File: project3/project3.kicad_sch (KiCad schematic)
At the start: 1 part

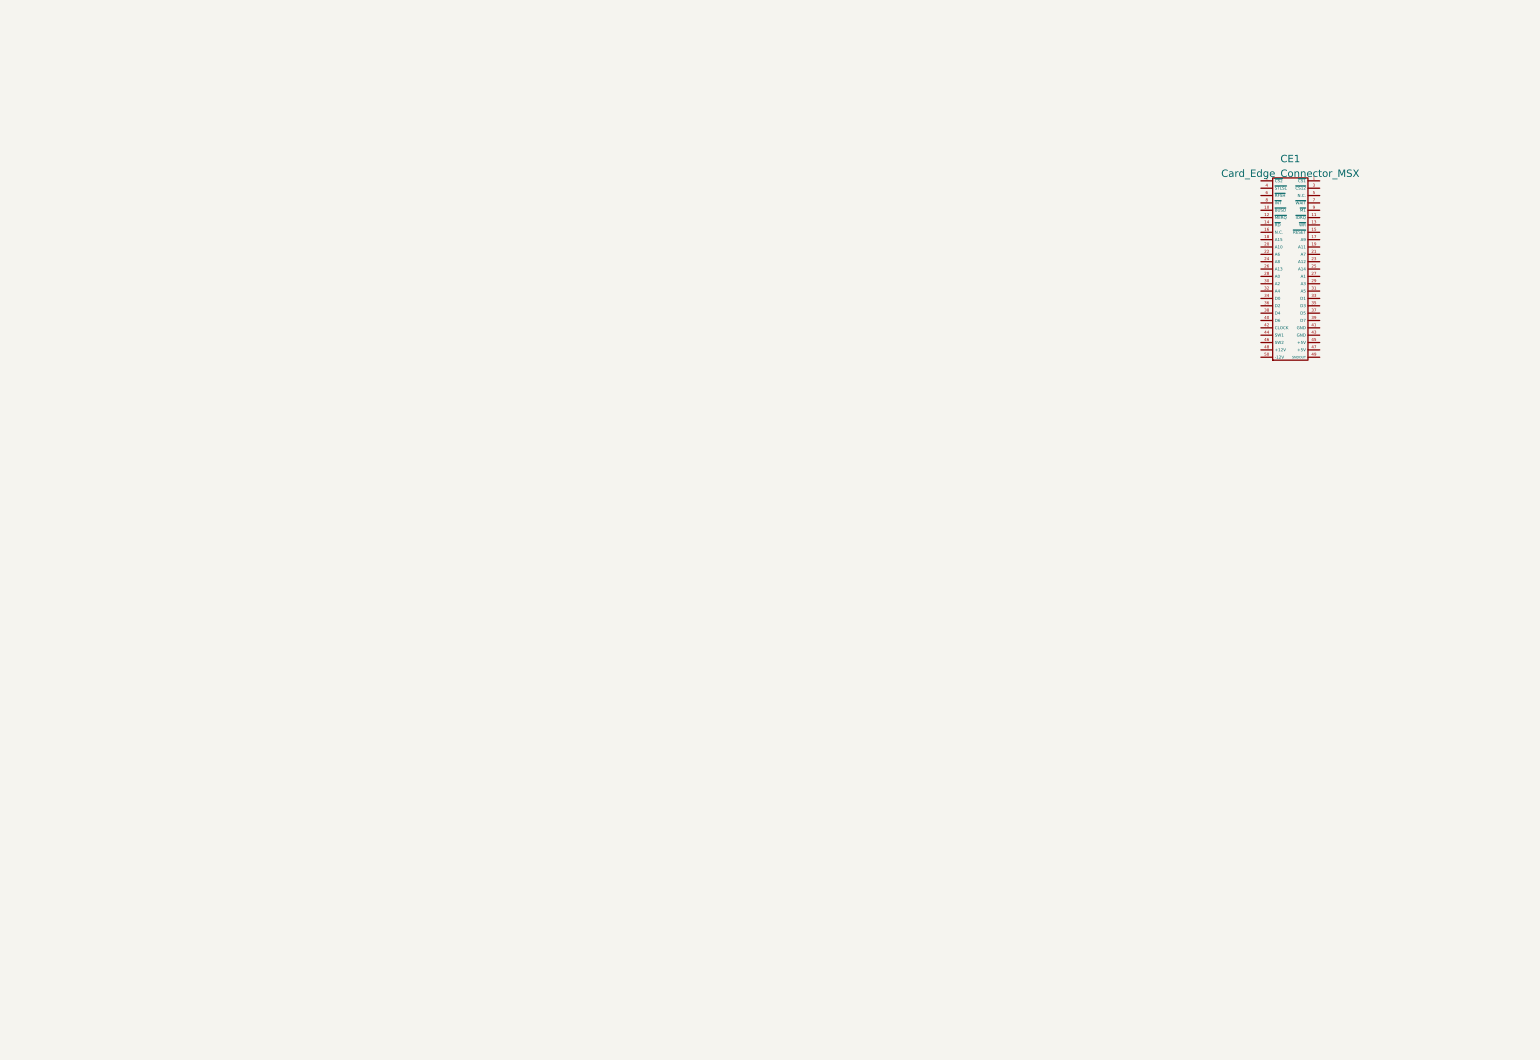
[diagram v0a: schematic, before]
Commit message: Created 4Mega ROM PCB - Change DIP32 type FLASH ROM - Optimal Logic Mega Rom Mapper.
Signed-off-by: Youngki Park <ykp7409@gmail.com>
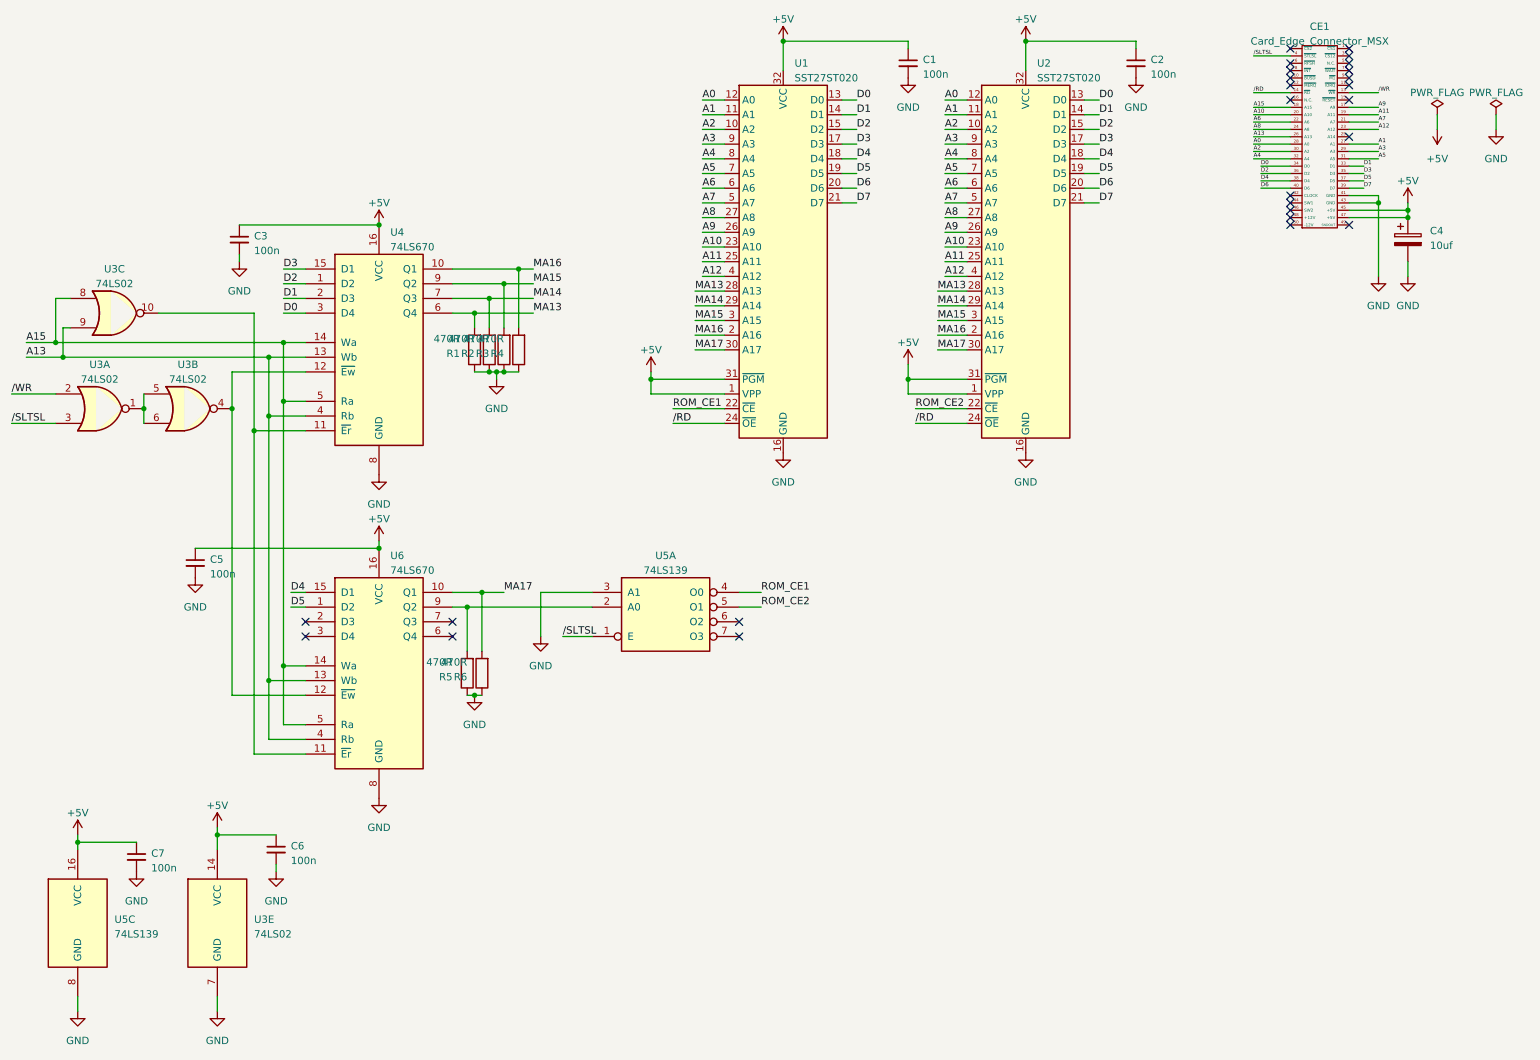
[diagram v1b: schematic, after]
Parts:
- added C1, C2, C3, C5, C6, C7: 100n, Capacitor_THT:C_Disc_D6.0mm_W2.5mm_P5.00mm, symbol Device:C_Small
- added C4: 10uf, Capacitor_THT:CP_Radial_D5.0mm_P2.50mm, symbol Device:C_Polarized
- added R1, R2, R3, R4, R5, R6: 470R, Resistor_THT:R_Axial_DIN0207_L6.3mm_D2.5mm_P10.16mm_Horizontal, symbol Device:R
- added U1, U2: SST27ST020, Package_DIP:DIP-32_W15.24mm_Socket, symbol Memory_Flash_Custom:SST27ST020
- added U3: 74LS02, Package_DIP:DIP-14_W7.62mm_Socket, symbol 74xx:74LS02
- added U4, U6: 74LS670, Package_DIP:DIP-16_W7.62mm_Socket, symbol 74xx:74LS670
- added U5: 74LS139, Package_DIP:DIP-16_W7.62mm_Socket, symbol 74xx:74LS139
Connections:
- net /WR: now reaches CE1.13 (~{WR})
- net /WR: now also U3.2
- net /RD: now reaches CE1.14 (~{RD})
- net /RD: now also U1.24 (~{OE}), U2.24 (~{OE})
- net A9: now reaches CE1.17 (A9)
- net A9: now also U1.26 (A9), U2.26 (A9)
- net A15: now reaches CE1.18 (A15)
- net A15: now also U3.8, U4.14 (Wa), U4.5 (Ra), U6.14 (Wa), U6.5 (Ra)
- net A11: now reaches CE1.19 (A11)
- net A11: now also U1.25 (A11), U2.25 (A11)
- net A10: now reaches CE1.20 (A10)
- net A10: now also U1.23 (A10), U2.23 (A10)
- net A7: now reaches CE1.21 (A7)
- net A7: now also U1.5 (A7), U2.5 (A7)
- net A6: now reaches CE1.22 (A6)
- net A6: now also U1.6 (A6), U2.6 (A6)
- net A12: now reaches CE1.23 (A12)
- net A12: now also U1.4 (A12), U2.4 (A12)
- net A8: now reaches CE1.24 (A8)
- net A8: now also U1.27 (A8), U2.27 (A8)
- net A13: now reaches CE1.26 (A13)
- net A13: now also U3.9, U4.13 (Wb), U4.4 (Rb), U6.13 (Wb), U6.4 (Rb)
- net A1: now reaches CE1.27 (A1)
- net A1: now also U1.11 (A1), U2.11 (A1)
- net A0: now reaches CE1.28 (A0)
- net A0: now also U1.12 (A0), U2.12 (A0)
- net A3: now reaches CE1.29 (A3)
- net A3: now also U1.9 (A3), U2.9 (A3)
- net A2: now reaches CE1.30 (A2)
- net A2: now also U1.10 (A2), U2.10 (A2)
- net A5: now reaches CE1.31 (A5)
- net A5: now also U1.7 (A5), U2.7 (A5)
- net A4: now reaches CE1.32 (A4)
- net A4: now also U1.8 (A4), U2.8 (A4)
- net D1: now reaches CE1.33 (D1)
- net D1: now also U1.14 (D1), U2.14 (D1), U4.2 (D3)
- net D0: now reaches CE1.34 (D0)
- net D0: now also U1.13 (D0), U2.13 (D0), U4.3 (D4)
- net D3: now reaches CE1.35 (D3)
- net D3: now also U1.17 (D3), U2.17 (D3), U4.15 (D1)
- net D2: now reaches CE1.36 (D2)
- net D2: now also U1.15 (D2), U2.15 (D2), U4.1 (D2)
- net D5: now reaches CE1.37 (D5)
- net D5: now also U1.19 (D5), U2.19 (D5), U6.1 (D2)
- net D4: now reaches CE1.38 (D4)
- net D4: now also U1.18 (D4), U2.18 (D4), U6.15 (D1)
- net D7: now reaches CE1.39 (D7)
- net D7: now also U1.21 (D7), U2.21 (D7)
- net /SLTSL: now reaches CE1.4 (~{STLSL})
- net /SLTSL: now also U3.3, U5.1 (E)
- net D6: now reaches CE1.40 (D6)
- net D6: now also U1.20 (D6), U2.20 (D6)
- net GND: now reaches CE1.41 (GND)
- net GND: now also CE1.43 (GND), C1.2, C2.2, C3.2, C4.2, C5.2, C6.2, C7.2, R1.1, R2.1, R3.1, R4.1, R5.1, R6.1, U1.16 (GND), U2.16 (GND), U3.7 (GND), U4.8 (GND), U5.3 (A1), U5.8 (GND), U6.8 (GND)
- net +5V: now reaches CE1.45 (+5V)
- net +5V: now also CE1.47 (+5V), C1.1, C2.1, C3.1, C4.1, C5.1, C6.1, C7.1, U1.1 (VPP), U1.31 (~{PGM}), U1.32 (VCC), U2.1 (VPP), U2.31 (~{PGM}), U2.32 (VCC), U3.14 (VCC), U4.16 (VCC), U5.16 (VCC), U6.16 (VCC)
- new net: U3.10, U4.11 (~{Er}), U6.11 (~{Er})
- new net: U3.4, U4.12 (~{Ew}), U6.12 (~{Ew})
- new net: R5.2, U5.2 (A0), U6.9 (Q2)
- new net: U3.1, U3.5, U3.6
- new net MA13: R1.2, U1.28 (A13), U2.28 (A13), U4.6 (Q4)
- new net MA14: R2.2, U1.29 (A14), U2.29 (A14), U4.7 (Q3)
- new net MA15: R3.2, U1.3 (A15), U2.3 (A15), U4.9 (Q2)
- new net MA16: R4.2, U1.2 (A16), U2.2 (A16), U4.10 (Q1)
- new net MA17: R6.2, U1.30 (A17), U2.30 (A17), U6.10 (Q1)
- new net ROM_CE1: U1.22 (~{CE}), U5.4 (O0)
- new net ROM_CE2: U2.22 (~{CE}), U5.5 (O1)
- no-connect marks 0 -> 26
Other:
- company: (none) -> SEC
- title: (none) -> 4M Mega Rom Card (KONAMI type)

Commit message: Modify the PCB layout
Signed-off-by: Youngki Park <ykp7409@gmail.com>
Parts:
- C1, C2, C3, C5, C6, C7: value 100n -> 0.1uF
- C4: value 10uf -> 10uF
- R1, R2, R3, R4, R5, R6: value 470R -> 470
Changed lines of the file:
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@@
       (effects (font (size 1.27 1.27)) (justify left))
     )
-    (property "Value" "100n" (at 171.45 28.5813 0)
+    (property "Value" "0.1uF" (at 171.45 28.5813 0)
       (effects (font (size 1.27 1.27)) (justify left))
     )
@@
       (effects (font (size 1.27 1.27)) (justify left))
     )
-    (property "Value" "100n" (at 210.82 28.5813 0)
+    (property "Value" "0.1uF" (at 210.82 28.5813 0)
       (effects (font (size 1.27 1.27)) (justify left))
     )
@@
       (effects (font (size 1.27 1.27)) (justify left))
     )
-    (property "Value" "470R" (at 96.52 74.295 0)
+    (property "Value" "470" (at 96.52 74.295 0)
       (effects (font (size 1.27 1.27)) (justify left))
     )
@@
       (effects (font (size 1.27 1.27)) (justify left))
     )
-    (property "Value" "100n" (at 62.23 164.4713 0)
+    (property "Value" "0.1uF" (at 62.23 164.4713 0)
       (effects (font (size 1.27 1.27)) (justify left))
     )
@@
       (effects (font (size 1.27 1.27)) (justify left))
     )
-    (property "Value" "470R" (at 90.17 130.175 0)
+    (property "Value" "470" (at 90.17 130.175 0)
       (effects (font (size 1.27 1.27)) (justify left))
     )
@@
       (effects (font (size 1.27 1.27)) (justify left))
     )
-    (property "Value" "470R" (at 91.44 74.295 0)
+    (property "Value" "470" (at 91.44 74.295 0)
       (effects (font (size 1.27 1.27)) (justify left))
     )
@@
       (effects (font (size 1.27 1.27)) (justify left))
     )
-    (property "Value" "100n" (at 55.88 59.0613 0)
+    (property "Value" "0.1uF" (at 55.88 59.0613 0)
       (effects (font (size 1.27 1.27)) (justify left))
     )
@@
       (effects (font (size 1.27 1.27)) (justify left))
     )
-    (property "Value" "470R" (at 99.06 74.295 0)
+    (property "Value" "470" (at 99.06 74.295 0)
       (effects (font (size 1.27 1.27)) (justify left))
     )
@@
       (effects (font (size 1.27 1.27)) (justify left))
     )
-    (property "Value" "470R" (at 92.71 130.175 0)
+    (property "Value" "470" (at 92.71 130.175 0)
       (effects (font (size 1.27 1.27)) (justify left))
     )
@@
       (effects (font (size 1.27 1.27)) (justify left))
     )
-    (property "Value" "100n" (at 48.26 114.9413 0)
+    (property "Value" "0.1uF" (at 48.26 114.9413 0)
       (effects (font (size 1.27 1.27)) (justify left))
     )
@@
       (effects (font (size 1.27 1.27)) (justify left))
     )
-    (property "Value" "100n" (at 38.1 165.7413 0)
+    (property "Value" "0.1uF" (at 38.1 165.7413 0)
       (effects (font (size 1.27 1.27)) (justify left))
     )
@@
       (effects (font (size 1.27 1.27)) (justify left))
     )
-    (property "Value" "10uf" (at 259.08 58.166 0)
+    (property "Value" "10uF" (at 259.08 58.166 0)
       (effects (font (size 1.27 1.27)) (justify left))
     )
@@
       (effects (font (size 1.27 1.27)) (justify left))
     )
-    (property "Value" "470R" (at 93.98 74.295 0)
-      (effects (font (size 1.27 1.27)) (justify left))
-    )
+    (property "Value" "470" (at 93.98 74.295 0)
+      (effects (font (size 1.27 1.27)) (justify left))
+    )
